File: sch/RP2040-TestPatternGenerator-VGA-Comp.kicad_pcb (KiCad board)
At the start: 2 copper layers, 21 x 12 mm, 29 parts, among them J1 DE15_Receptacle_HighDensity_M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, J2 CVBS, SW1 SW_Push, SW2 SW_Push, U1 rp2040-zero, U2 AD724JRZ, Y1 3.579545

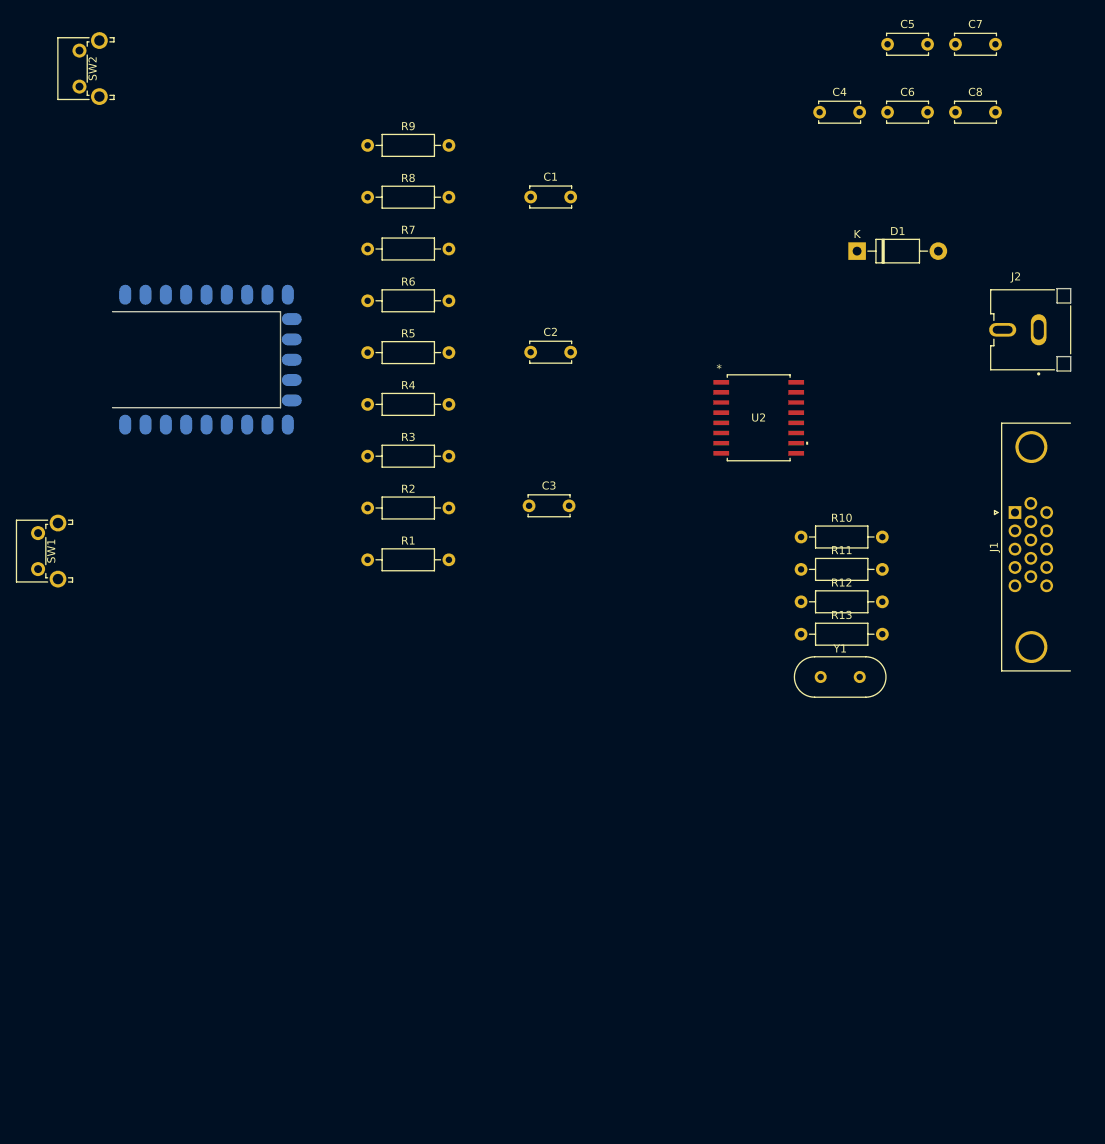
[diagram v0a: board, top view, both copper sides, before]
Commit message: finalised PCB size/holes based on 100x66x38mm enclosure
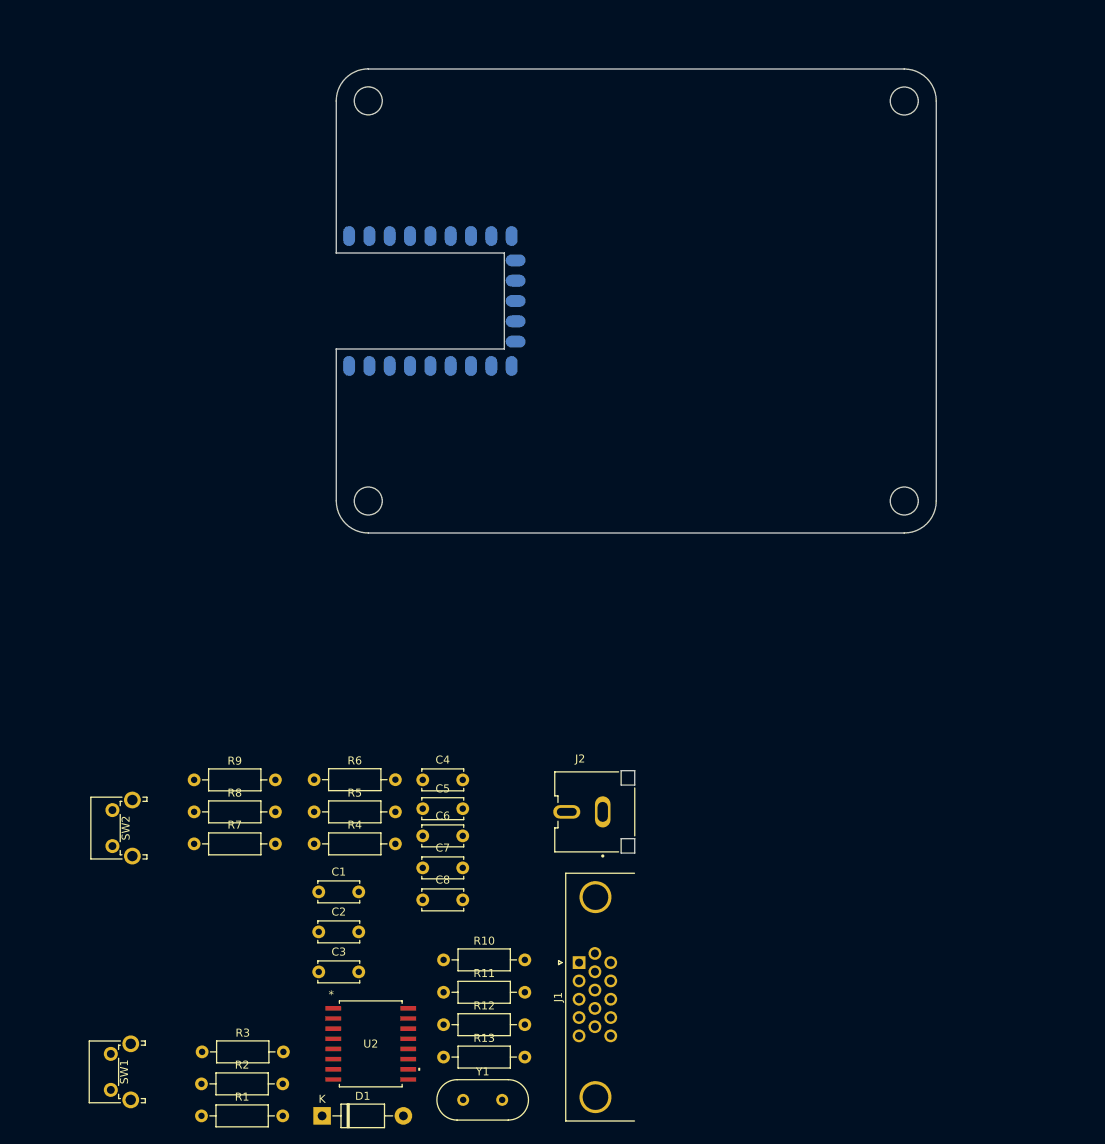
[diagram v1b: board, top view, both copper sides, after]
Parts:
- moved D1 127.1 mm to (98.2, 190.9)
- moved C7 122.6 mm to (110.8, 159.9)
- moved C8 118.9 mm to (110.8, 163.9)
- moved C5 111.8 mm to (110.8, 152.5)
- moved C6 107.5 mm to (110.8, 155.9)
- moved C4 97.1 mm to (110.8, 148.9)
- moved SW2 95.0 mm to (72.0, 157.1)
- moved U2 92.1 mm to (104.3, 181.9)
- moved C1 90.8 mm to (97.8, 162.9)
- moved R9 82.2 mm to (82.2, 148.9)
- moved J2 81.2 mm to (133.3, 152.9)
- moved R8 79.8 mm to (82.2, 152.9)
- moved J1 78.3 mm to (130.3, 171.7)
- moved R7 77.5 mm to (82.2, 156.9)
- moved R3 77.3 mm to (83.2, 182.9)
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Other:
- board size 21 x 12 mm -> 75 x 58 mm

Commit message: actual final dimensions
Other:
- board size 75 x 58 mm -> 82 x 58 mm
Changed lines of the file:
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@@
     )
   )
+  (gr_arc (start 100 64) (mid 101.171573 61.171573) (end 104 60)
+    (stroke (width 0.1) (type default)) (layer "Edge.Cuts"))
   (gr_line (start 100.01 83) (end 100 83)
     (stroke (width 0.1) (type default)) (layer "Edge.Cuts"))
-  (gr_arc (start 175 114) (mid 173.828427 116.828427) (end 171 118)
+  (gr_arc (start 182 114) (mid 180.828427 116.828427) (end 178 118)
     (stroke (width 0.1) (type default)) (layer "Edge.Cuts"))
   (gr_line (start 100 114) (end 100 95)
     (stroke (width 0.1) (type default)) (layer "Edge.Cuts"))
-  (gr_arc (start 100.000001 64) (mid 101.1659 61.161213) (end 104 59.983969)
-    (stroke (width 0.1) (type default)) (layer "Edge.Cuts"))
-  (gr_line (start 175 64) (end 175 114)
+  (gr_line (start 182 64) (end 182 114)
     (stroke (width 0.1) (type default)) (layer "Edge.Cuts"))
   (gr_line (start 100.01 83) (end 100 83)
     (stroke (width 0.1) (type default)) (layer "Edge.Cuts"))
-  (gr_circle (center 104 63.984) (end 105.75 63.984)
+  (gr_circle (center 107.25 64) (end 109 64)
     (stroke (width 0.1) (type default)) (fill none) (layer "Edge.Cuts"))
   (gr_arc (start 104 118) (mid 101.171573 116.828427) (end 100 114)
     (stroke (width 0.1) (type default)) (layer "Edge.Cuts"))
-  (gr_line (start 104 60) (end 171 60)
+  (gr_line (start 104 60) (end 178 60)
     (stroke (width 0.1) (type default)) (layer "Edge.Cuts"))
   (gr_line (start 100 83) (end 100 64)
@@
   (gr_line (start 100.01 95) (end 100 95)
     (stroke (width 0.1) (type default)) (layer "Edge.Cuts"))
-  (gr_circle (center 104 114) (end 105.75 114)
+  (gr_circle (center 107.25 114) (end 109 114)
     (stroke (width 0.1) (type default)) (fill none) (layer "Edge.Cuts"))
-  (gr_line (start 171 118) (end 104 118)
+  (gr_line (start 178 118) (end 104 118)
     (stroke (width 0.1) (type default)) (layer "Edge.Cuts"))
-  (gr_arc (start 171 60) (mid 173.828427 61.171573) (end 175 64)
+  (gr_arc (start 178 60) (mid 180.828427 61.171573) (end 182 64)
     (stroke (width 0.1) (type default)) (layer "Edge.Cuts"))
-  (gr_circle (center 171 114) (end 172.75 114)
+  (gr_circle (center 174.25 114) (end 176 114)
     (stroke (width 0.1) (type default)) (fill none) (layer "Edge.Cuts"))
-  (gr_circle (center 171 64) (end 172.75 64)
+  (gr_circle (center 174.25 64) (end 176 64)
     (stroke (width 0.1) (type default)) (fill none) (layer "Edge.Cuts"))
   (gr_line (start 100.01 95) (end 100.005 95)

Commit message: finalised PCB size/holes based on 100x60x25mm enclosure
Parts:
- moved J2 97.9 mm to (190.0, 73.0)
- moved J1 97.9 mm to (187.0, 91.8)
- moved SW2 87.7 mm to (102.7, 75.0)
- moved SW1 84.0 mm to (102.7, 109.5)
- moved U1 1.00 mm to (111.8, 90.0)
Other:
- board size 82 x 58 mm -> 94 x 54 mm
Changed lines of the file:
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@@
   )
   (footprint "Button_Switch_THT:SW_Tactile_SPST_Angled_PTS645Vx58-2LFS" (layer "F.Cu")
-    (at 71.819669 187.61 90)
+    (at 102.7125 109.5 90)
     (descr "tactile switch SPST right angle, PTS645VL58-2 LFS")
     (tags "tactile switch SPST angled PTS645VL58-2 LFS C&K Button")
@@
   )
   (footprint "Connector_Dsub:DSUB-15-HD_Female_Horizontal_P2.29x1.98mm_EdgePinOffset3.03mm_Housed_MountingHolesOffset4.94mm" (layer "F.Cu")
-    (at 130.349669 171.7 90)
+    (at 187.04 91.84 90)
     (descr "15-pin D-Sub connector, horizontal/angled (90 deg), THT-mount, female, pitch 2.29x1.98mm, pin-PCB-offset 3.0300000000000002mm, distance of mounting holes 25mm, distance of mounting holes to PCB edge 4.9399999999999995mm, see https://disti-assets.s3.amazonaws.com/tonar/files/datasheets/16730.pdf")
     (tags "15-pin D-Sub connector horizontal angled 90deg THT female pitch 2.29x1.98mm pin-PCB-offset 3.0300000000000002mm mounting-holes-distance 25mm mounting-hole-offset 25mm")
@@
   )
   (footprint "RCA:CUI_RCJ-044" (layer "F.Cu")
-    (at 133.309669 152.86)
+    (at 190 73)
     (property "Sheetfile" "RP2040-TestPatternGenerator-VGA-Comp.kicad_sch")
     (property "Sheetname" "")
@@
   )
   (footprint "Button_Switch_THT:SW_Tactile_SPST_Angled_PTS645Vx58-2LFS" (layer "F.Cu")
-    (at 72.022169 157.135 90)
+    (at 102.7125 75 90)
     (descr "tactile switch SPST right angle, PTS645VL58-2 LFS")
     (tags "tactile switch SPST angled PTS645VL58-2 LFS C&K Button")
@@
   )
   (footprint "RP2040-Zero:rp2040-zero-smd" (layer "B.Cu")
-    (at 111.76 89 -90)
+    (at 111.76 90 -90)
     (property "Sheetfile" "RP2040-TestPatternGenerator-VGA-Comp.kicad_sch")
     (property "Sheetname" "")
@@
     )
   )
-  (gr_arc (start 100 64) (mid 101.171573 61.171573) (end 104 60)
+  (gr_line (start 100.01 84) (end 100 84)
     (stroke (width 0.1) (type default)) (layer "Edge.Cuts"))
-  (gr_line (start 100.01 83) (end 100 83)
+  (gr_line (start 100 115) (end 100 96)
     (stroke (width 0.1) (type default)) (layer "Edge.Cuts"))
-  (gr_arc (start 182 114) (mid 180.828427 116.828427) (end 178 118)
+  (gr_line (start 194 65) (end 194 115)
     (stroke (width 0.1) (type default)) (layer "Edge.Cuts"))
-  (gr_line (start 100 114) (end 100 95)
+  (gr_arc (start 100 65) (mid 100.585786 63.585786) (end 102 63)
     (stroke (width 0.1) (type default)) (layer "Edge.Cuts"))
-  (gr_line (start 182 64) (end 182 114)
+  (gr_line (start 100.01 84) (end 100 84)
     (stroke (width 0.1) (type default)) (layer "Edge.Cuts"))
-  (gr_line (start 100.01 83) (end 100 83)
+  (gr_arc (start 102 117) (mid 100.585786 116.414214) (end 100 115)
     (stroke (width 0.1) (type default)) (layer "Edge.Cuts"))
-  (gr_circle (center 107.25 64) (end 109 64)
+  (gr_circle (center 102 65) (end 103.45 65)
     (stroke (width 0.1) (type default)) (fill none) (layer "Edge.Cuts"))
-  (gr_arc (start 104 118) (mid 101.171573 116.828427) (end 100 114)
+  (gr_line (start 102 63) (end 192 63)
     (stroke (width 0.1) (type default)) (layer "Edge.Cuts"))
-  (gr_line (start 104 60) (end 178 60)
+  (gr_line (start 100 84) (end 100 65)
     (stroke (width 0.1) (type default)) (layer "Edge.Cuts"))
-  (gr_line (start 100 83) (end 100 64)
+  (gr_line (start 100.01 96) (end 100 96)
     (stroke (width 0.1) (type default)) (layer "Edge.Cuts"))
-  (gr_line (start 100.01 95) (end 100 95)
+  (gr_arc (start 194 115) (mid 193.414214 116.414214) (end 192 117)
     (stroke (width 0.1) (type default)) (layer "Edge.Cuts"))
-  (gr_circle (center 107.25 114) (end 109 114)
+  (gr_circle (center 102 115) (end 103.45 115)
     (stroke (width 0.1) (type default)) (fill none) (layer "Edge.Cuts"))
-  (gr_line (start 178 118) (end 104 118)
+  (gr_line (start 192 117) (end 102 117)
     (stroke (width 0.1) (type default)) (layer "Edge.Cuts"))
-  (gr_arc (start 178 60) (mid 180.828427 61.171573) (end 182 64)
+  (gr_arc (start 192 63) (mid 193.414214 63.585786) (end 194 65)
     (stroke (width 0.1) (type default)) (layer "Edge.Cuts"))
-  (gr_circle (center 174.25 114) (end 176 114)
+  (gr_circle (center 192 115) (end 193.45 115)
     (stroke (width 0.1) (type default)) (fill none) (layer "Edge.Cuts"))
-  (gr_circle (center 174.25 64) (end 176 64)
+  (gr_circle (center 192 65) (end 193.45 65)
     (stroke (width 0.1) (type default)) (fill none) (layer "Edge.Cuts"))
-  (gr_line (start 100.01 95) (end 100.005 95)
+  (gr_line (start 100.01 96) (end 100.005 96)
     (stroke (width 0.1) (type default)) (layer "Edge.Cuts"))
 )

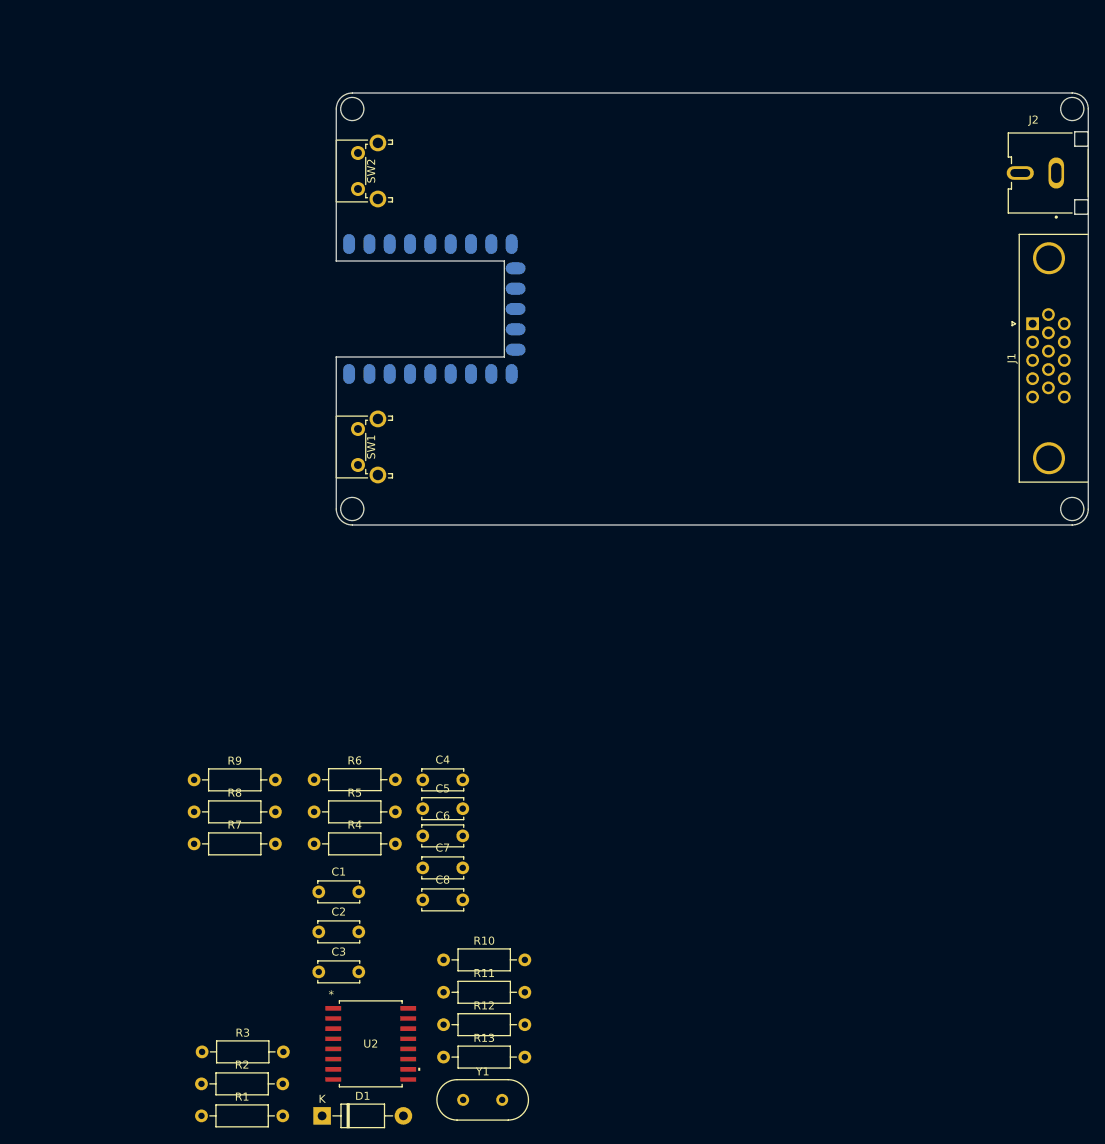
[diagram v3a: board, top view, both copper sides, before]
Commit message: first attempt at positioning all components before traces
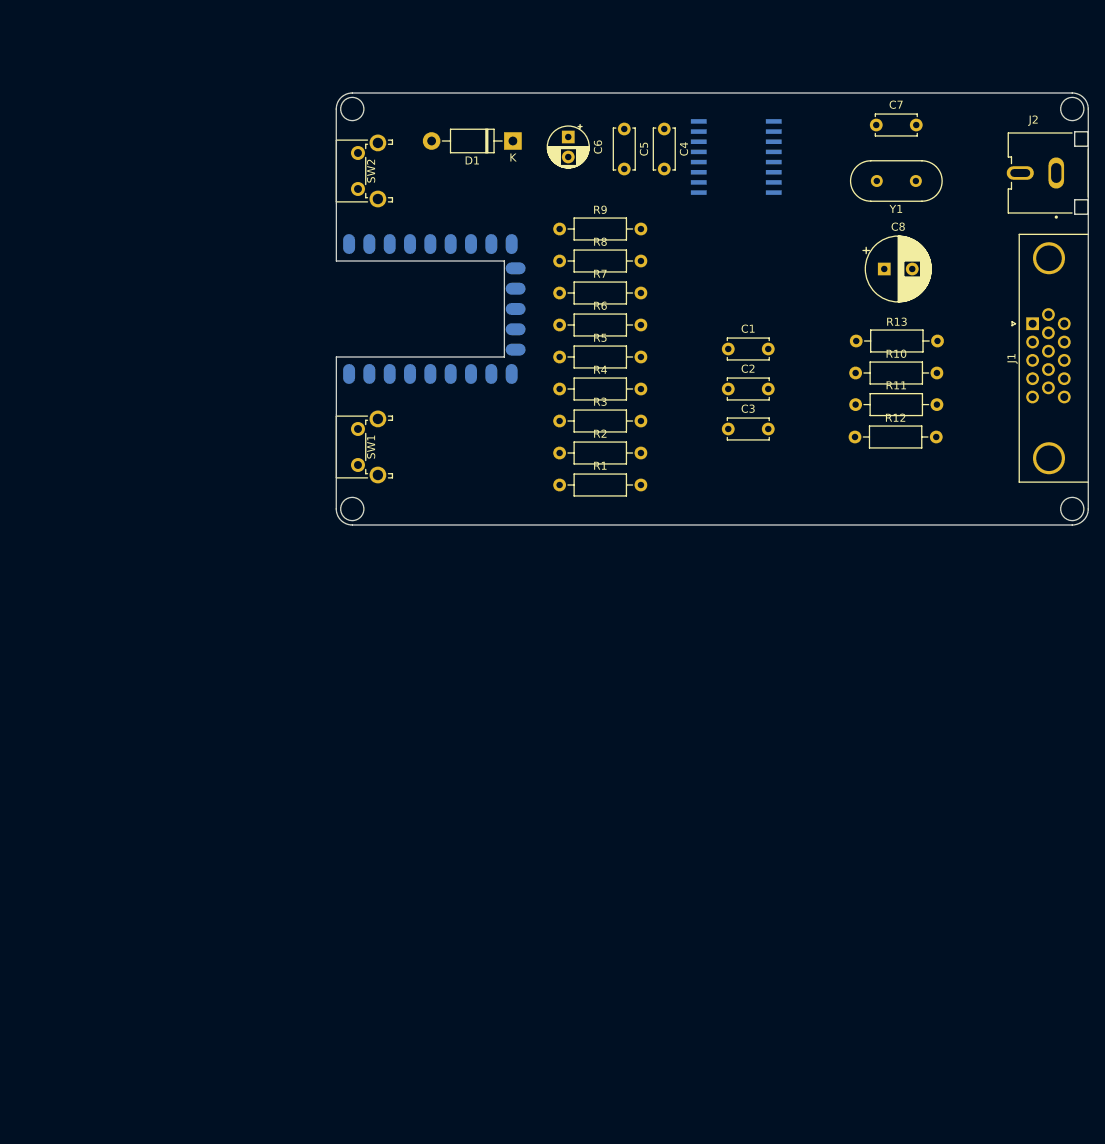
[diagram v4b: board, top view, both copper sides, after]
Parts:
- C6: footprint Capacitor_THT:C_Disc_D5.0mm_W2.5mm_P5.00mm -> Capacitor_THT:CP_Radial_D5.0mm_P2.50mm
- C8: footprint Capacitor_THT:C_Disc_D5.0mm_W2.5mm_P5.00mm -> Capacitor_THT:CP_Radial_D8.0mm_P3.50mm
- U2: moved to B.Cu
- moved Y1 128.0 mm to (172.4, 74.0), turned to 180 degrees
- moved D1 124.2 mm to (122.1, 69.0), turned to 180 degrees
- moved U2 119.9 mm to (150.0, 71.0), turned to 180 degrees
- moved C7 108.8 mm to (167.5, 67.0)
- moved R13 103.3 mm to (165.0, 94.0)
- moved C8 97.7 mm to (168.5, 85.0)
- moved R1 90.7 mm to (127.9, 112.0)
- moved R2 90.7 mm to (127.9, 108.0)
- moved R3 90.6 mm to (127.9, 104.0)
- moved R11 89.7 mm to (164.9, 102.0)
- moved R12 89.7 mm to (164.8, 106.0)
- moved R10 89.6 mm to (164.9, 98.0)
- moved C6 89.2 mm to (129.0, 68.5), turned to -90 degrees
- moved C5 88.6 mm to (136.0, 67.5), turned to -90 degrees
- moved C4 86.8 mm to (141.0, 67.5), turned to -90 degrees
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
